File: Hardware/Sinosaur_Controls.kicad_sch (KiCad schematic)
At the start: 30 parts, among them J1 Conn_01x12_Male, J10 Sine1InvOut, J11 FM2Out, J12 RampOut, J13 SwellOut, J14 FM3Out, J2 Conn_01x16_Male, J3 Conn_01x12_Male, J4 Conn_01x16_Male, J5 WavetablePosA, J6 WavetablePosB, J7 Sine1Out, J8 Sine2Out, J9 Sine3Out

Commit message: Started control layout
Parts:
- added D10, D11, D7, D8, D9: LED_BGAR, LED_THT:LED_D5.0mm-4_RGB, symbol Device:LED_BGAR
- D6: footprint (none) -> LED_THT:LED_D5.0mm-4_RGB
- J1, J3: footprint Connector_PinHeader_2.54mm:PinHeader_1x12_P2.54mm_Vertical -> Connector_PinSocket_2.54mm:PinSocket_1x12_P2.54mm_Vertical
- J14: renamed from J5; value WavetablePosA -> ClockIn
- J2, J4: footprint Connector_PinHeader_2.54mm:PinHeader_1x16_P2.54mm_Vertical -> Connector_PinSocket_2.54mm:PinSocket_1x16_P2.54mm_Vertical
- J9: renamed from J6; value WavetablePosB -> GateIn
- renumbered J14 to J12, J7 to J5, J8 to J6, J9 to J7, J12 to J8, Ramp_Level_Trm to Ramp_Level_Trm1, Ramp_Rate_Pot to Ramp_Rate_Pot1, Swell_LeveL_Trm to Swell_LeveL_Trm1, Swell_Rate_Pot to Swell_Rate_Pot1
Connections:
- net +3.3V: now also D6.3 (A), D10.3 (A), D11.3 (A), D7.3 (A), D8.3 (A), D9.3 (A)
- net Sine1_Ramp_Lvl_LED: now also D7.1 (BK)
- net Sine1_Ramp_Rate_LED: now also D6.1 (BK)
- net Sine1_Swell_Lvl_LED: now also D7.4 (RK)
- net Sine1_Swell_Rate_LED: now also D6.4 (RK)
- net Sine2_Ramp_Lvl_LED: now also D9.1 (BK)
- net Sine2_Ramp_Rate_LED: now also D8.1 (BK)
- net Sine2_Swell_Lvl_LED: now also D9.4 (RK)
- net Sine2_Swell_Rate_LED: now also D8.4 (RK)
- net Sine3_Ramp_Lvl_LED: now also D11.1 (BK)
- net Sine3_Ramp_Rate_LED: now also D10.1 (BK)
- net Sine3_Swell_Lvl_LED: now also D11.4 (RK)
- net Sine3_Swell_Rate_LED: now also D10.4 (RK)
- no-connect marks 8 -> 14

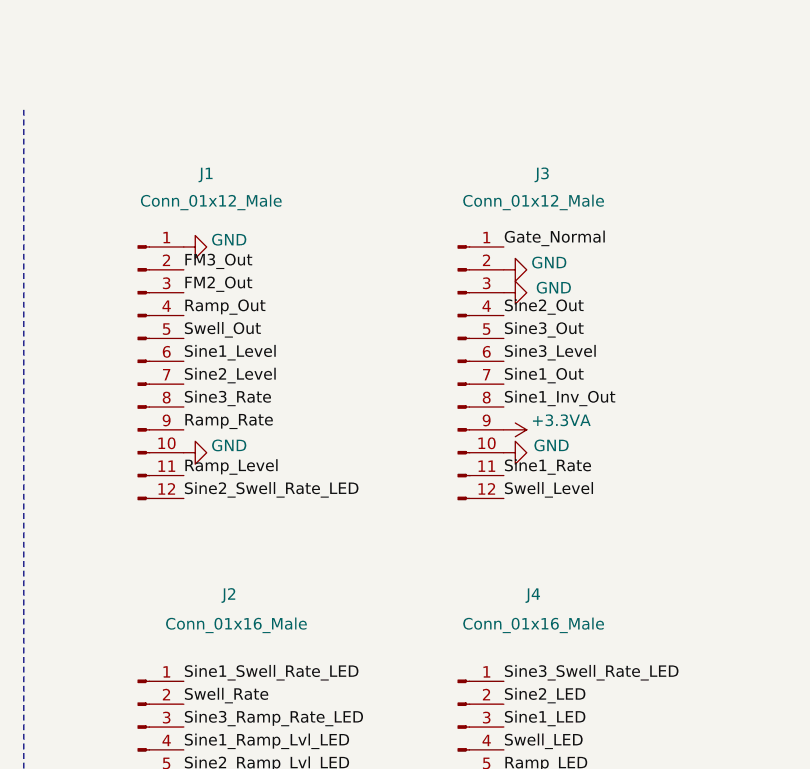
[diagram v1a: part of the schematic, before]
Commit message: Control PCB wiring
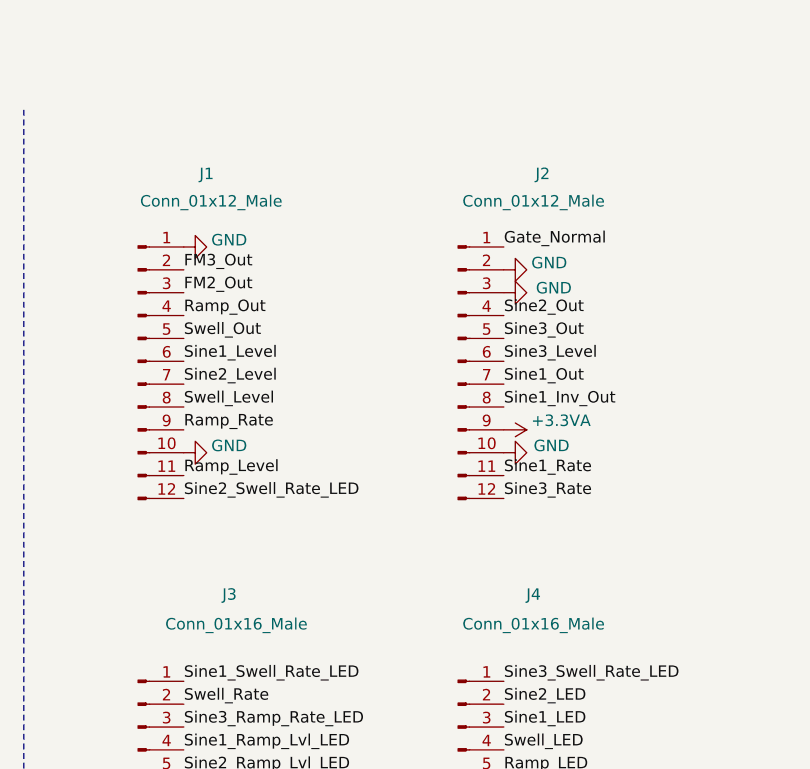
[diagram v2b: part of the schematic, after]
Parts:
- renumbered J3 to J2, J2 to J3
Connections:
- net Sine3_Rate: now also J2.12 (Pin_12); no longer J1.8 (Pin_8)
- net Swell_Level: now also J1.8 (Pin_8); no longer J2.12 (Pin_12)
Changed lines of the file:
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@@
 	)
 	(label "Swell_Level"
-		(at 255.27 55.88 0)
+		(at 219.71 45.72 0)
 		(fields_autoplaced yes)
 		(effects
@@
 	)
 	(label "Sine3_Rate"
-		(at 219.71 45.72 0)
+		(at 255.27 55.88 0)
 		(fields_autoplaced yes)
 		(effects
@@
 		(on_board yes)
 		(dnp no)
-		(property "Reference" "J3"
+		(property "Reference" "J2"
 			(at 259.588 19.812 0)
 			(effects
@@
 			(project "Sinosaur_Controls"
 				(path "/00778401-a8b8-4a7c-bae7-c4fa7505df01"
-					(reference "J3")
+					(reference "J2")
 					(unit 1)
 				)
@@
 		(on_board yes)
 		(dnp no)
-		(property "Reference" "J2"
+		(property "Reference" "J3"
 			(at 224.79 66.548 0)
 			(effects
@@
 			(project "Sinosaur_Controls"
 				(path "/00778401-a8b8-4a7c-bae7-c4fa7505df01"
-					(reference "J2")
+					(reference "J3")
 					(unit 1)
 				)

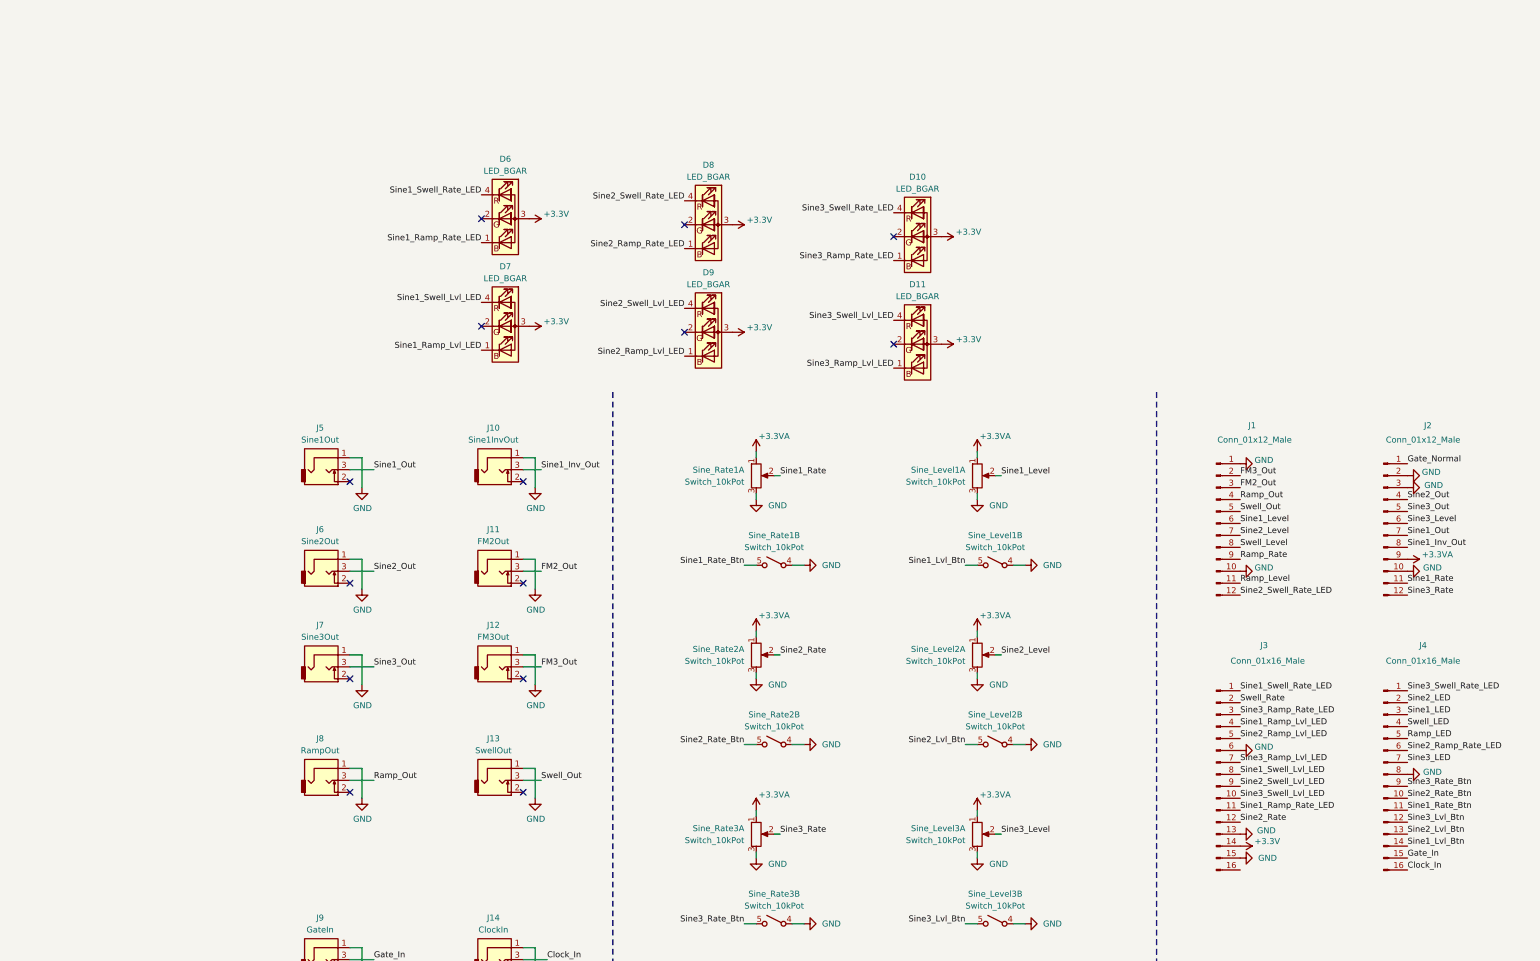
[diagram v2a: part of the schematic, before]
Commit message: Updates to LEDs
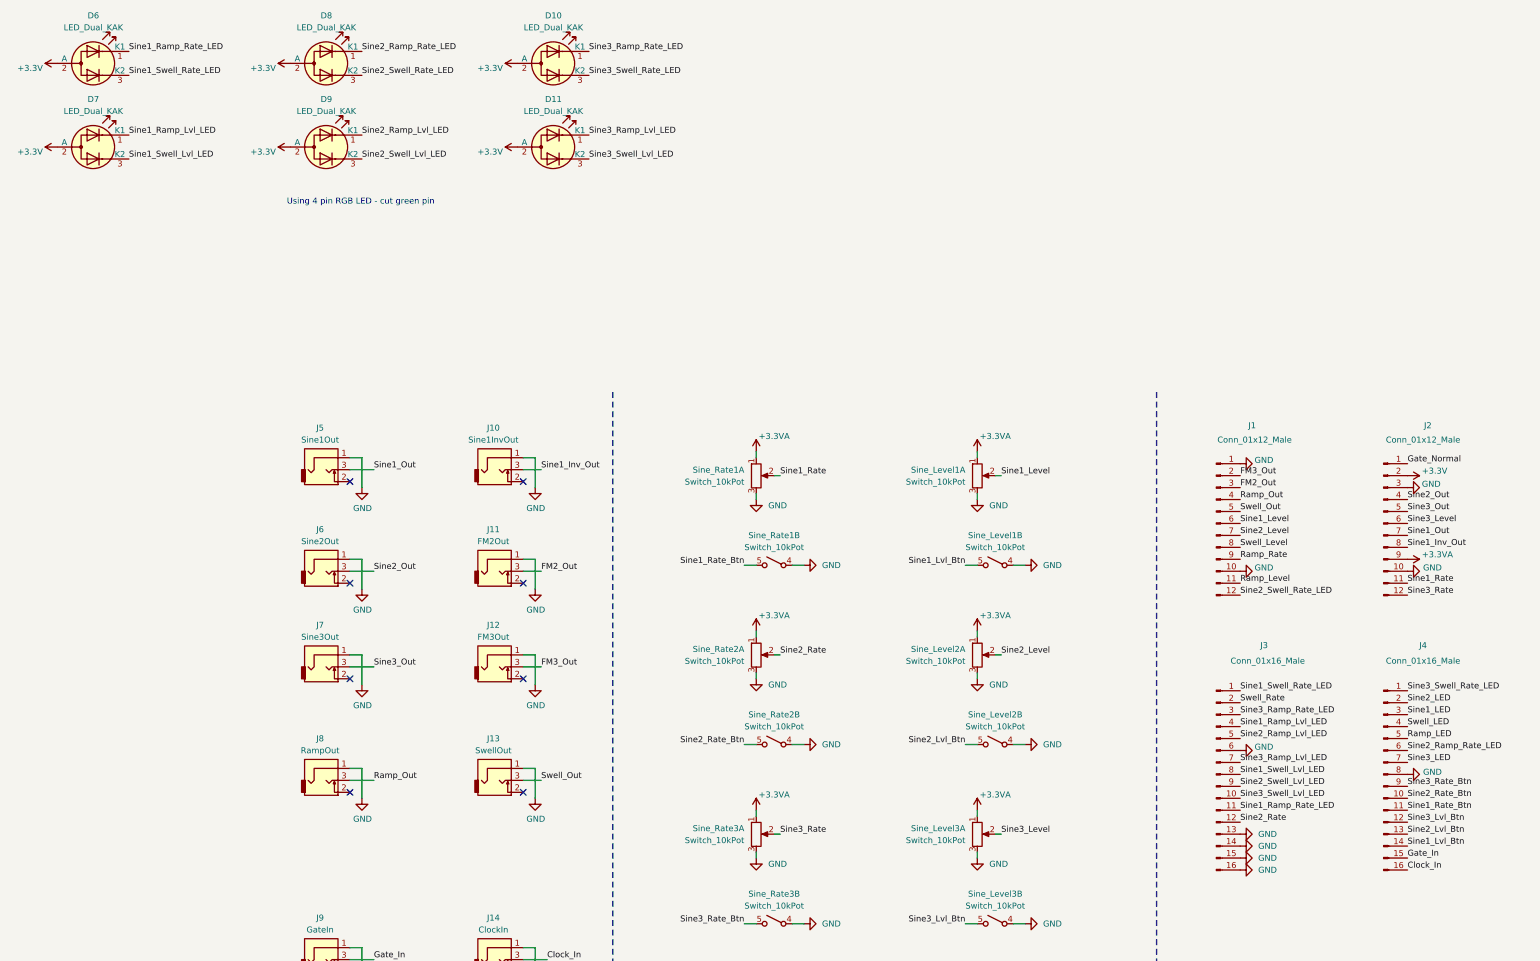
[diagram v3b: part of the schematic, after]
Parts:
- removed D10, D11, D6, D7, D8, D9: LED_BGAR, LED_THT:LED_D5.0mm-4_RGB, symbol Device:LED_BGAR
- added D10, D11, D6, D7, D8, D9: LED_Dual_KAK, Custom_Footprints:LED_D3.0mm-3, symbol Device:LED_Dual_KAK
- D1, D2, D3, D4, D5: footprint LED_THT:LED_D3.0mm_FlatTop -> Custom_Footprints:LED_D3.0mm
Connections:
- net +3.3V: now also J2.2 (Pin_2), D10.2 (A), D11.2 (A), D6.2 (A), D7.2 (A), D8.2 (A), D9.2 (A); no longer J3.14 (Pin_14)
- net GND: now also J3.14 (Pin_14), J3.16 (Pin_16); no longer J2.2 (Pin_2)
- net Sine1_Ramp_Lvl_LED: now also D7.1 (K1)
- net Sine1_Ramp_Rate_LED: now also D6.1 (K1)
- net Sine1_Swell_Lvl_LED: now also D7.3 (K2)
- net Sine1_Swell_Rate_LED: now also D6.3 (K2)
- net Sine2_Ramp_Lvl_LED: now also D9.1 (K1)
- net Sine2_Ramp_Rate_LED: now also D8.1 (K1)
- net Sine2_Swell_Lvl_LED: now also D9.3 (K2)
- net Sine2_Swell_Rate_LED: now also D8.3 (K2)
- net Sine3_Ramp_Lvl_LED: now also D11.1 (K1)
- net Sine3_Ramp_Rate_LED: now also D10.1 (K1)
- net Sine3_Swell_Lvl_LED: now also D11.3 (K2)
- net Sine3_Swell_Rate_LED: now also D10.3 (K2)
- no-connect marks 14 -> 8
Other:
- note added: "Using 4 pin RGB LED - cut green pin"

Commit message: Gerber production
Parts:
- J1, J2: symbol Connector:Conn_01x12_Pin -> Connector:Conn_01x12_Socket
- J3, J4: symbol Connector:Conn_01x16_Pin -> Connector:Conn_01x16_Socket
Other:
- note added: "Dual LEDs"
- note added: "LEDs"
- note added: "Switched Potentiometers"
- moved on the sheet: D1, D10, D11, D2, D3, D4, D5, D6, D7, D8, D9, J10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

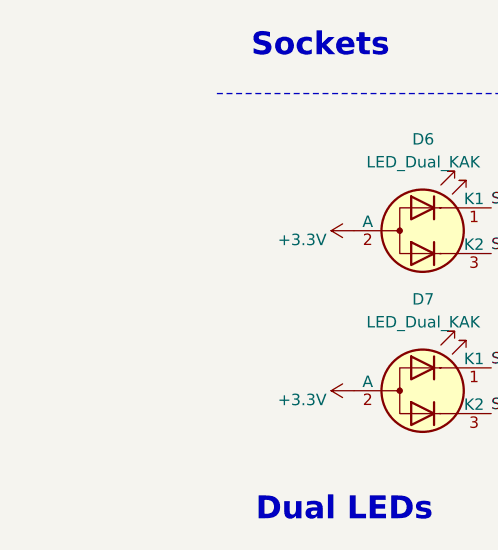
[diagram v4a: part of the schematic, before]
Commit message: Hardware working; started adding modulation code
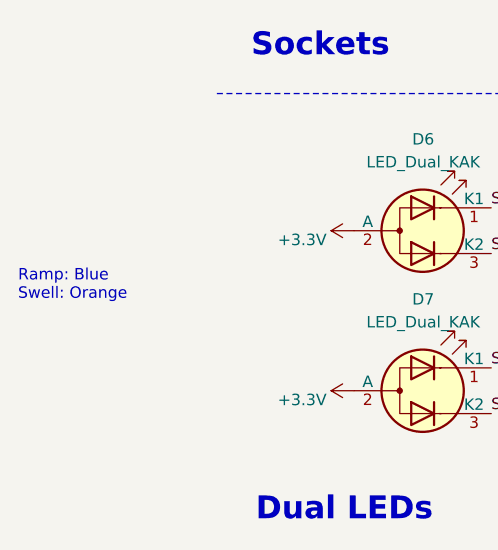
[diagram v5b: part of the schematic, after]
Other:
- note added: "Ramp: Blue Swell: Orange"
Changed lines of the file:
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@@
+		)
+	)
+	(text "Ramp: Blue\nSwell: Orange"
+		(exclude_from_sim no)
+		(at -9.398 167.386 0)
+		(effects
+			(font
+				(size 1.27 1.27)
+			)
+			(justify left)
 		)
 	)
